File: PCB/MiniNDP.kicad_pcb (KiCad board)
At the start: 2 copper layers, 60 x 34 mm, 25 parts, among them J1 Conn_02x20_Odd_Even, U1 AS6C8008_TSOPII, U2 HC238, U3 HC4040, U4 FCT841

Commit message: ez1m minor pcb & silkscreen changes
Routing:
- net /~{WR}: track 33.9 -> 35.3 mm
- net /BUS_A8: track 21.7 -> 20.7 mm
- net /BUS_A9: track 17.1 -> 17.8 mm
- net /AD3: track 29.6 -> 30.2 mm
- net GND: vias 71 -> 97
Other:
- board text added: "To reinstall RAMDSK from device after hard reset. RAMxxx.CO must be the first file in bank 0."
- board text removed: "Bootstrap RAMDSK from BANK 0. For BANK 1 change OUT129 to OUT133. RAM100.CO or RAM200.CO must be the first file in the bank."

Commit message: minindp ez1m sl1m ez512 u1m pcbs trace spacing & gnd paths
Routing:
- net GND: vias 97 -> 98
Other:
- board text added: "bank0-3: P=129,133,137,141 block0-255: OUT P,N read byte: D=INP(131) write byte: OUT 131,D"
- board text removed: "bank0-3: P=129,133,137,141 block0-255: OUT P,N read byte: N=INP(131) write byte: OUT 131,N"

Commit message: ez1m fillet tracks
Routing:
- net /RAMRST: track 60.5 -> 59.2 mm
- net VBUS: track 83.2 -> 84.1 mm
- net /AD6: track 40.2 -> 39.6 mm

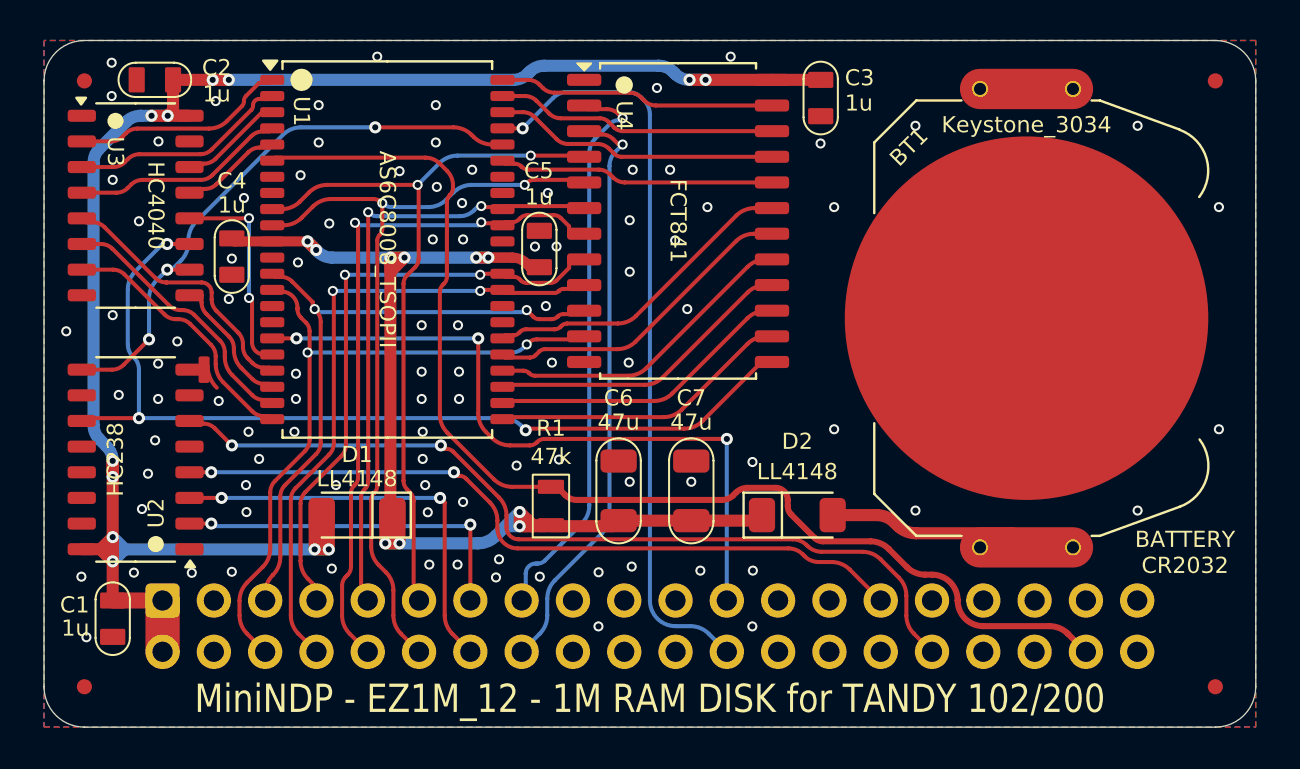
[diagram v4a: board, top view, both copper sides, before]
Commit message: ez1m microscopic trace spacing/curves adjustments
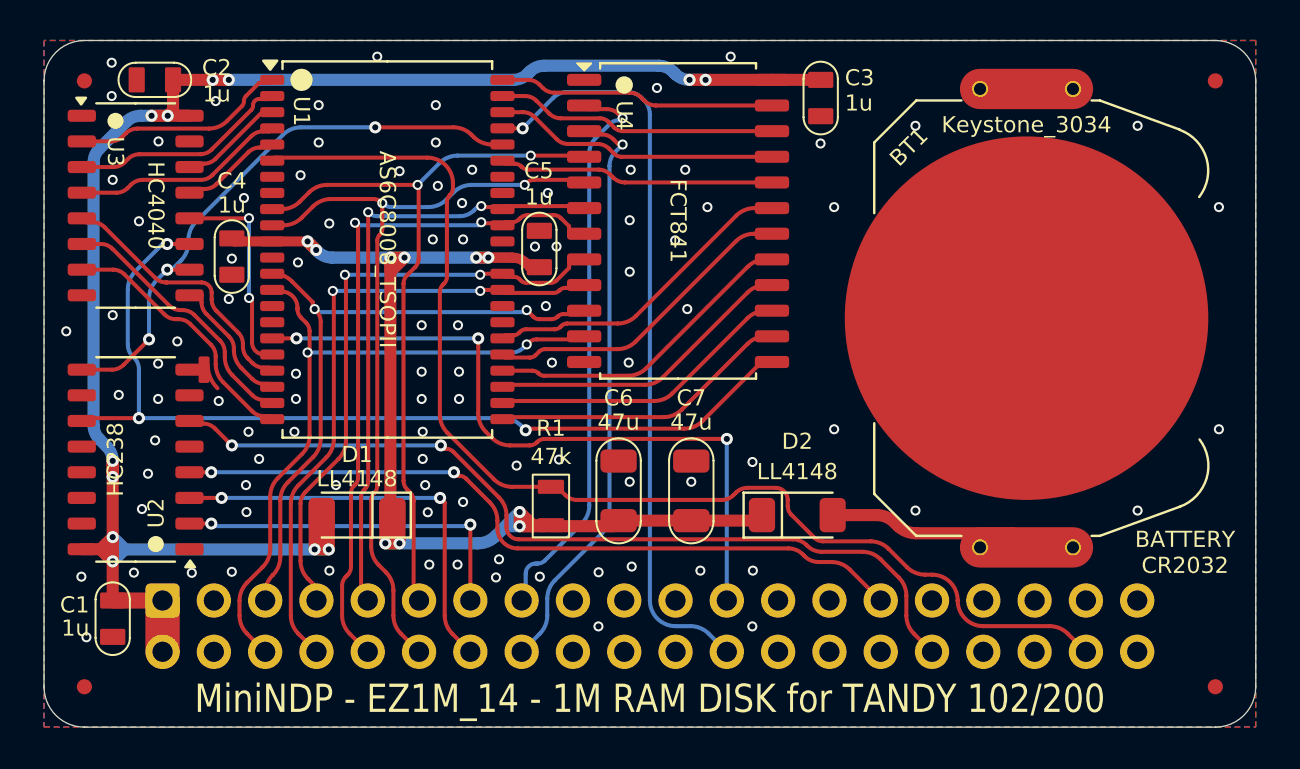
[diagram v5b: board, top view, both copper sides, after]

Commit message: ez1m 014 silkscreen
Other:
- board text added: "BASIC to bootstrap RAMxxx.CO previously saved as the first file in bank 0"
- board text removed: "To reinstall RAMDSK from device after hard reset. RAMxxx.CO must be the first file in bank 0."
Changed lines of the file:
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@@
 		)
 	)
-	(gr_text "To reinstall RAMDSK from device after hard reset.\nRAMxxx.CO must be the first file in bank 0."
-		(at 175.445 94.705 0)
+	(gr_text "BASIC to bootstrap RAMxxx.CO previously saved as the first file in bank 0"
+		(at 151.95 95.213 0)
 		(layer "B.SilkS")
 		(effects
@@
 				(thickness 0.14)
 			)
-			(justify left mirror)
+			(justify mirror)
 		)
 	)
 	(gr_text "1M RAM DISK for\nTANDY 102/200"
-		(at 132.519 88.228 0)
+		(at 132.519 88.99 0)
 		(layer "B.SilkS")
 		(effects
@@
 	)
 	(gr_text "${COMMENT1} - ${REVISION}"
-		(at 151.95 91.525 0)
+		(at 151.95 92.8 0)
 		(layer "B.SilkS")
 		(effects
@@
 	)
 	(gr_text "${TITLE}"
-		(at 151.95 88.477 0)
+		(at 151.95 89.117 0)
 		(layer "B.SilkS")
 		(effects

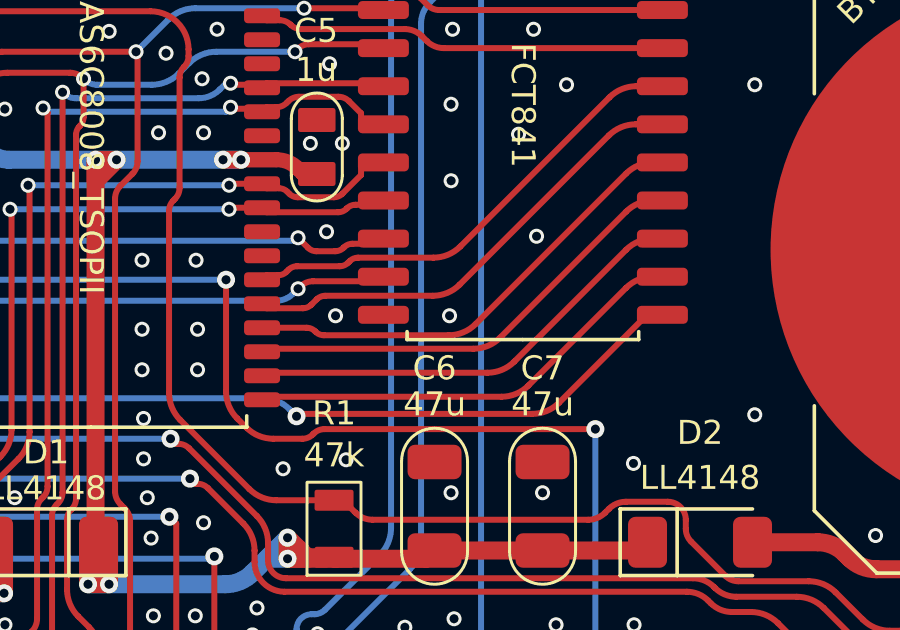
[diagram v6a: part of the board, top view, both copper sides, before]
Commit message: u1M vias near C1 pad, silkscreen, smooth traces
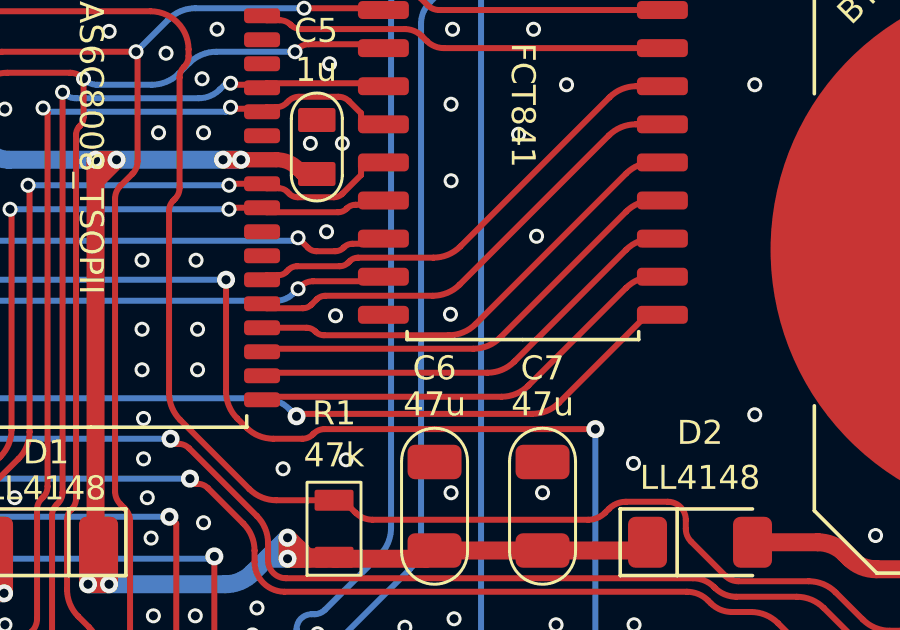
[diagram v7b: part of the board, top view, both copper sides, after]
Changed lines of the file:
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@@
 	)
 	(via
-		(at 150.9 101.975)
+		(at 150.93 101.925)
 		(size 0.5)
 		(drill 0.3)

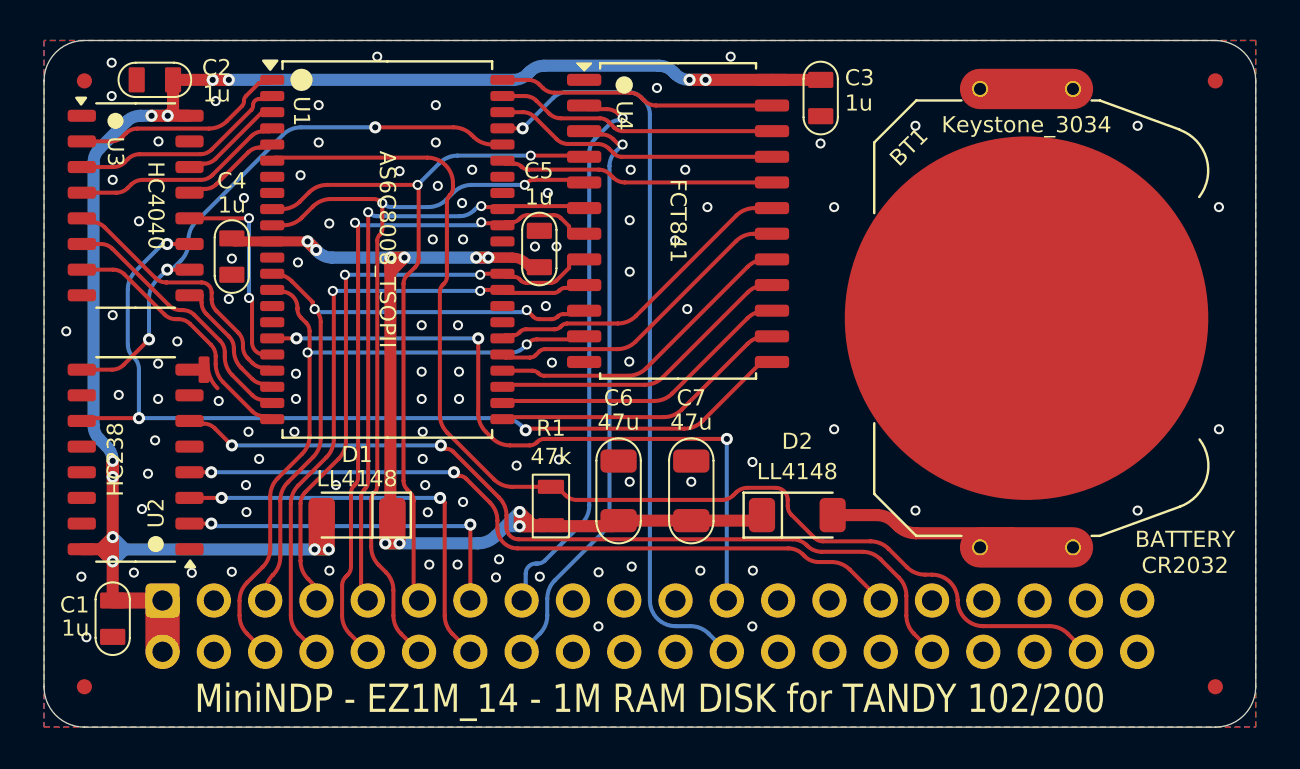
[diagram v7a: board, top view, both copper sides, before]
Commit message: simplify covers, strengthen battery holders, silkscreen, readme
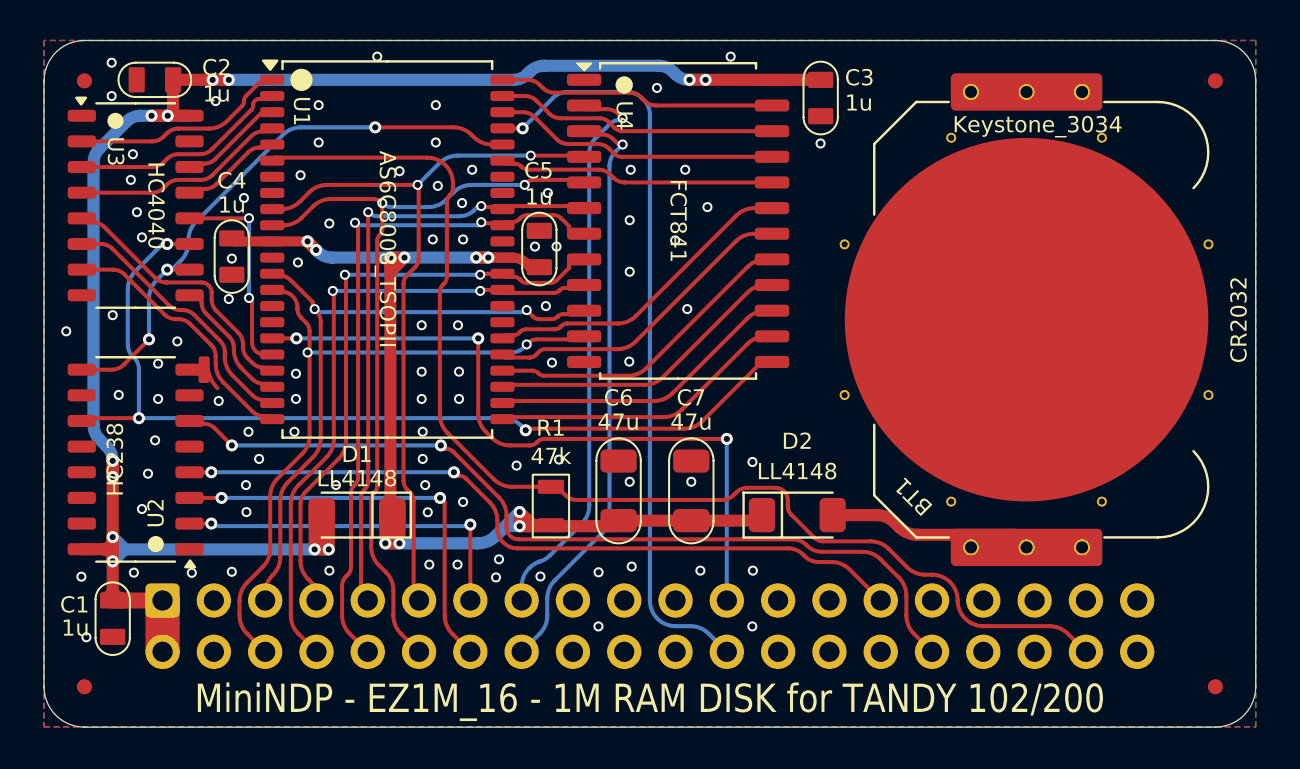
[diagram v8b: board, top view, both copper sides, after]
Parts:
- removed REF** (x4): pth_nail, 000_LOCAL:pth_nail
- BT1: footprint 000_LOCAL:Keystone_3028_3034 -> 000_LOCAL:Keystone_3028_3034_bkw
- moved BT1 0.07 mm to (170.6, 99.8)
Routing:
- net GND: vias 98 -> 91
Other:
- board text added: "CR2032"
- board text added: "bank 0-3: P=129,133,137,141 block 0-255: OUT P,N read byte: D=INP(131) write byte: OUT 131,D"
- board text removed: "bank0-3: P=129,133,137,141 block0-255: OUT P,N read byte: D=INP(131) write byte: OUT 131,D"
